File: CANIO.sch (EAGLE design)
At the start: 9 parts

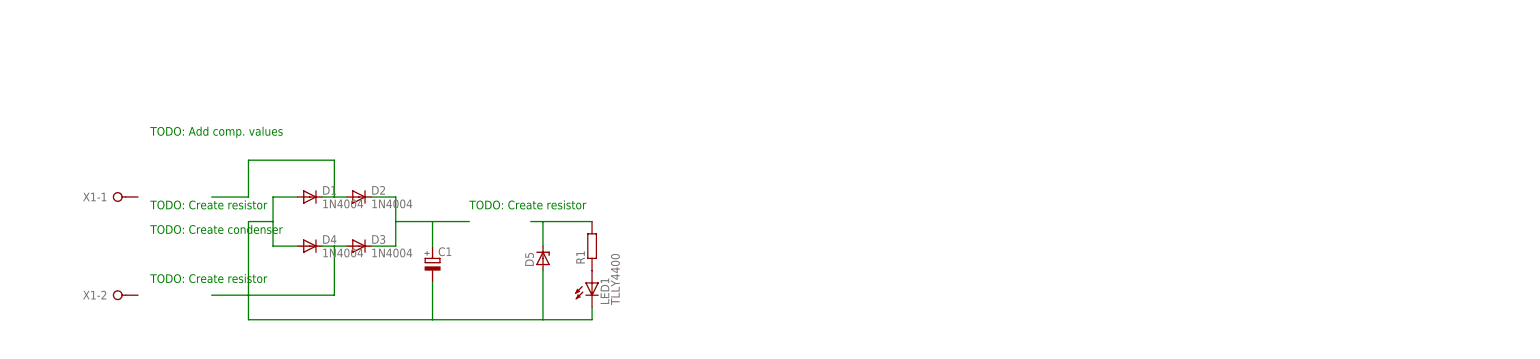
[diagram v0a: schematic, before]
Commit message: adding sensor connector
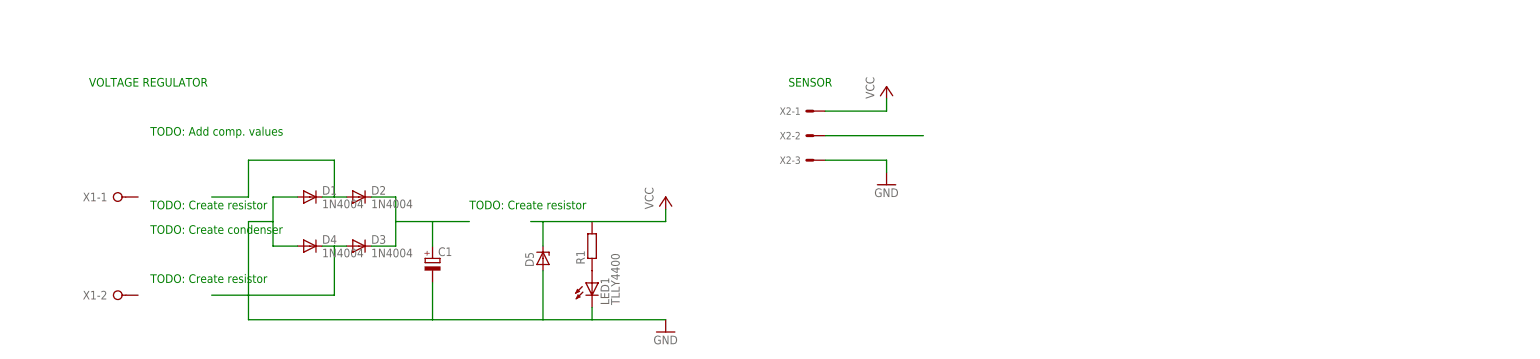
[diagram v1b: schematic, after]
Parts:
- added X2: (no value), con-molex:KK-156-3
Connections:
- removed net N$5: D5.C, R1.2
- new net GND: C1.-, D1.A, D4.A, D5.A, LED1.C, X2-3.S
- new net VCC: D5.C, R1.2, X2-1.S
- net N$4: now also X2-2.S; no longer C1.-, D1.A, D4.A, D5.A, LED1.C
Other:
- note added: "SENSOR"
- note added: "VOLTAGE REGULATOR"
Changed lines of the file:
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@@
 <part name="R1" library="rcl" library_urn="urn:adsk.eagle:library:334" deviceset="R-EU_" device="0204/5"/>
 <part name="LED1" library="led" library_urn="urn:adsk.eagle:library:259" deviceset="TLLY4400" device=""/>
+<part name="P+1" library="supply1" library_urn="urn:adsk.eagle:library:371" deviceset="VCC" device=""/>
+<part name="GND1" library="supply1" library_urn="urn:adsk.eagle:library:371" deviceset="GND" device=""/>
+<part name="X2" library="con-molex" library_urn="urn:adsk.eagle:library:165" deviceset="KK-156-3" device=""/>
+<part name="P+2" library="supply1" library_urn="urn:adsk.eagle:library:371" deviceset="VCC" device=""/>
+<part name="GND2" library="supply1" library_urn="urn:adsk.eagle:library:371" deviceset="GND" device=""/>
 </parts>
 <sheets>
@@
 <text x="76.2" y="40.64" size="1.778" layer="91">TODO: Create resistor</text>
 <text x="10.16" y="55.88" size="1.778" layer="91">TODO: Add comp. values</text>
+<text x="-2.54" y="66.04" size="1.778" layer="91">VOLTAGE REGULATOR</text>
+<text x="142.24" y="66.04" size="1.778" layer="91">SENSOR</text>
 </plain>
 <instances>
@@
 <instance part="R1" gate="G$1" x="101.6" y="33.02" rot="R90"/>
 <instance part="LED1" gate="G$1" x="101.6" y="25.4"/>
+<instance part="P+1" gate="VCC" x="116.84" y="43.18"/>
+<instance part="GND1" gate="1" x="116.84" y="15.24"/>
+<instance part="X2" gate="-1" x="147.32" y="60.96" rot="R180"/>
+<instance part="X2" gate="-2" x="147.32" y="55.88" rot="R180"/>
+<instance part="X2" gate="-3" x="147.32" y="50.8" rot="R180"/>
+<instance part="P+2" gate="VCC" x="162.56" y="66.04"/>
+<instance part="GND2" gate="1" x="162.56" y="45.72"/>
 </instances>
 <busses>
@@
 </segment>
 </net>
-<net name="N$4" class="0">
+<net name="N$6" class="0">
+<segment>
+<pinref part="R1" gate="G$1" pin="1"/>
+<pinref part="LED1" gate="G$1" pin="A"/>
+</segment>
+</net>
+<net name="VCC" class="0">
+<segment>
+<wire x1="88.9" y1="38.1" x2="91.44" y2="38.1" width="0.1524" layer="91"/>
+<wire x1="91.44" y1="38.1" x2="91.44" y2="33.02" width="0.1524" layer="91"/>
+<pinref part="D5" gate="G$1" pin="C"/>
+<pinref part="R1" gate="G$1" pin="2"/>
+<wire x1="101.6" y1="38.1" x2="91.44" y2="38.1" width="0.1524" layer="91"/>
+<pinref part="P+1" gate="VCC" pin="VCC"/>
+<wire x1="101.6" y1="38.1" x2="116.84" y2="38.1" width="0.1524" layer="91"/>
+<wire x1="116.84" y1="38.1" x2="116.84" y2="40.64" width="0.1524" layer="91"/>
+</segment>
+<segment>
+<pinref part="X2" gate="-1" pin="S"/>
+<pinref part="P+2" gate="VCC" pin="VCC"/>
+<wire x1="149.86" y1="60.96" x2="162.56" y2="60.96" width="0.1524" layer="91"/>
+<wire x1="162.56" y1="60.96" x2="162.56" y2="63.5" width="0.1524" layer="91"/>
+</segment>
+</net>
+<net name="GND" class="0">
 <segment>
 <pinref part="D4" gate="1" pin="A"/>
@@
 <wire x1="91.44" y1="17.78" x2="101.6" y2="17.78" width="0.1524" layer="91"/>
 <wire x1="101.6" y1="17.78" x2="101.6" y2="20.32" width="0.1524" layer="91"/>
+<pinref part="GND1" gate="1" pin="GND"/>
+<wire x1="116.84" y1="17.78" x2="101.6" y2="17.78" width="0.1524" layer="91"/>
+</segment>
+<segment>
+<pinref part="X2" gate="-3" pin="S"/>
+<pinref part="GND2" gate="1" pin="GND"/>
+<wire x1="149.86" y1="50.8" x2="162.56" y2="50.8" width="0.1524" layer="91"/>
+<wire x1="162.56" y1="50.8" x2="162.56" y2="48.26" width="0.1524" layer="91"/>
 </segment>
 </net>
-<net name="N$5" class="0">
+<net name="N$4" class="0">
 <segment>
-<wire x1="88.9" y1="38.1" x2="91.44" y2="38.1" width="0.1524" layer="91"/>
-<wire x1="91.44" y1="38.1" x2="91.44" y2="33.02" width="0.1524" layer="91"/>
-<pinref part="D5" gate="G$1" pin="C"/>
-<pinref part="R1" gate="G$1" pin="2"/>
-<wire x1="101.6" y1="38.1" x2="91.44" y2="38.1" width="0.1524" layer="91"/>
+<pinref part="X2" gate="-2" pin="S"/>
+<wire x1="149.86" y1="55.88" x2="170.18" y2="55.88" width="0.1524" layer="91"/>
 </segment>
 </net>
-<net name="N$6" class="0">
-<segment>
-<pinref part="R1" gate="G$1" pin="1"/>
-<pinref part="LED1" gate="G$1" pin="A"/>
-</segment>
-</net>

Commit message: adding sensor robustness and moc3021
Sensor robustness:
+NPN transistor, base from sensor [0-3v]

MOC3021:
+Special protection (ripple) for inductive load
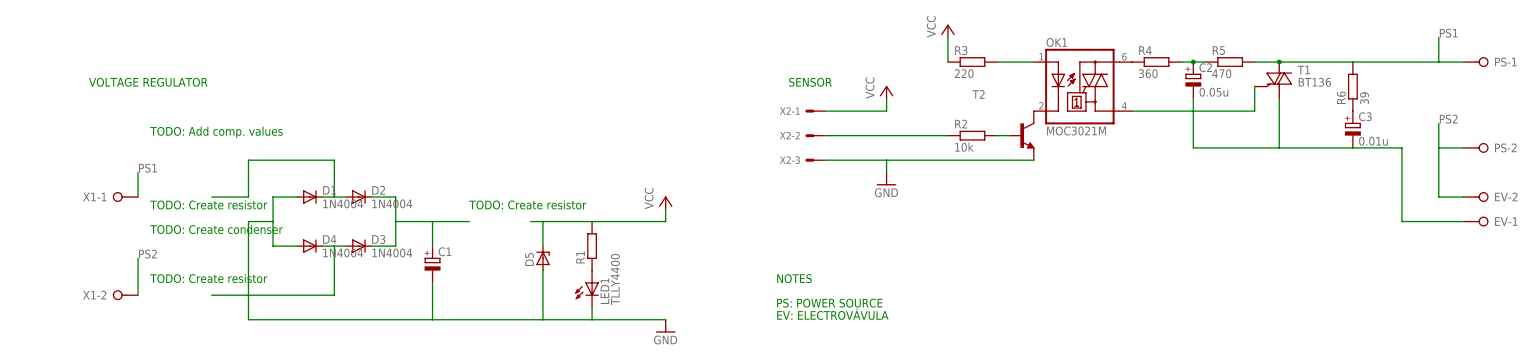
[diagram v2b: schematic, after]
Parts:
- added C2: 0.05u, rcl:CPOL-EUB45181A
- added C3: 0.01u, rcl:CPOL-EUB45181A
- added EV, PS: (no value), con-wago-508:W237-02P
- added OK1: MOC3021M, optocoupler:MOC3021M
- added R2: 10k, resistor:R-EU_0204/7
- added R3: 220, resistor:R-EU_0204/7
- added R4: 360, rcl:R-EU_0204/7
- added R5: 470, rcl:R-EU_0204/7
- added R6: 39, rcl:R-EU_0204/7
- added T1: BT136, triac:BT136
- added T2: (no value), transistor:-NPN-TO92
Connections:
- new net N$10: C2.+, R4.2, R5.1
- new net N$12: OK1.A1, T1.G
- new net N$13: C3.+, R6.1
- new net N$14: C2.-, C3.-, EV-1.KL, T1.A1
- new net N$5: R2.2, T2.B
- new net N$7: OK1.C, T2.C
- new net N$8: OK1.A, R3.2
- new net N$9: OK1.A2, R4.1
- new net PS1: PS-1.KL, R5.2, R6.2, T1.A2, X1-1.KL
- new net PS2: EV-2.KL, PS-2.KL, X1-2.KL
- net GND: now also T2.E
- net N$4: now also R2.1
- net VCC: now also R3.1
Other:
- note added: "EV: ELECTROVÁVULA"
- note added: "NOTES"
- note added: "PS: POWER SOURCE"
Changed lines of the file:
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@@
 <part name="P+2" library="supply1" library_urn="urn:adsk.eagle:library:371" deviceset="VCC" device=""/>
 <part name="GND2" library="supply1" library_urn="urn:adsk.eagle:library:371" deviceset="GND" device=""/>
+<part name="OK1" library="optocoupler" library_urn="urn:adsk.eagle:library:320" deviceset="MOC30*M" device="" technology="21"/>
+<part name="R2" library="resistor" library_urn="urn:adsk.eagle:library:348" deviceset="R-EU_" device="0204/7" value="10k"/>
+<part name="T1" library="triac" library_urn="urn:adsk.eagle:library:403" deviceset="BT136" device=""/>
+<part name="T2" library="transistor" library_urn="urn:adsk.eagle:library:402" deviceset="*-NPN-" device="TO92"/>
+<part name="R3" library="resistor" library_urn="urn:adsk.eagle:library:348" deviceset="R-EU_" device="0204/7" value="220"/>
+<part name="P+3" library="supply1" library_urn="urn:adsk.eagle:library:371" deviceset="VCC" device=""/>
+<part name="R4" library="rcl" library_urn="urn:adsk.eagle:library:334" deviceset="R-EU_" device="0204/7" value="360"/>
+<part name="R5" library="rcl" library_urn="urn:adsk.eagle:library:334" deviceset="R-EU_" device="0204/7" value="470"/>
+<part name="R6" library="rcl" library_urn="urn:adsk.eagle:library:334" deviceset="R-EU_" device="0204/7" value="39"/>
+<part name="C2" library="rcl" library_urn="urn:adsk.eagle:library:334" deviceset="CPOL-EU" device="B45181A" value="0.05u"/>
+<part name="C3" library="rcl" library_urn="urn:adsk.eagle:library:334" deviceset="CPOL-EU" device="B45181A" value="0.01u"/>
+<part name="PS" library="con-wago-508" library_urn="urn:adsk.eagle:library:196" deviceset="W237-02P" device=""/>
+<part name="EV" library="con-wago-508" library_urn="urn:adsk.eagle:library:196" deviceset="W237-02P" device=""/>
 </parts>
 <sheets>
@@
 <text x="-2.54" y="66.04" size="1.778" layer="91">VOLTAGE REGULATOR</text>
 <text x="142.24" y="66.04" size="1.778" layer="91">SENSOR</text>
+<text x="139.7" y="20.32" size="1.778" layer="91">PS: POWER SOURCE</text>
+<text x="139.7" y="25.4" size="1.778" layer="91">NOTES</text>
+<text x="139.7" y="17.78" size="1.778" layer="91">EV: ELECTROVÁVULA</text>
 </plain>
 <instances>
@@
 <instance part="P+2" gate="VCC" x="162.56" y="66.04"/>
 <instance part="GND2" gate="1" x="162.56" y="45.72"/>
+<instance part="OK1" gate="-1" x="203.2" y="66.04"/>
+<instance part="R2" gate="G$1" x="180.34" y="55.88"/>
+<instance part="T1" gate="-1" x="243.84" y="66.04"/>
+<instance part="T2" gate="G$1" x="190.5" y="55.88"/>
+<instance part="R3" gate="G$1" x="180.34" y="71.12"/>
+<instance part="P+3" gate="VCC" x="175.26" y="78.74"/>
+<instance part="R4" gate="G$1" x="218.44" y="71.12"/>
+<instance part="R5" gate="G$1" x="233.68" y="71.12"/>
+<instance part="R6" gate="G$1" x="259.08" y="66.04" rot="R90"/>
+<instance part="C2" gate="G$1" x="226.06" y="68.58"/>
+<instance part="C3" gate="G$1" x="259.08" y="58.42"/>
+<instance part="PS" gate="-1" x="287.02" y="71.12" rot="R180"/>
+<instance part="PS" gate="-2" x="287.02" y="53.34" rot="R180"/>
+<instance part="EV" gate="-1" x="287.02" y="38.1" rot="R180"/>
+<instance part="EV" gate="-2" x="287.02" y="43.18" rot="R180"/>
 </instances>
 <busses>
@@
 <wire x1="149.86" y1="60.96" x2="162.56" y2="60.96" width="0.1524" layer="91"/>
 <wire x1="162.56" y1="60.96" x2="162.56" y2="63.5" width="0.1524" layer="91"/>
+</segment>
+<segment>
+<pinref part="R3" gate="G$1" pin="1"/>
+<pinref part="P+3" gate="VCC" pin="VCC"/>
+<wire x1="175.26" y1="76.2" x2="175.26" y2="71.12" width="0.1524" layer="91"/>
 </segment>
 </net>
@@
 <wire x1="149.86" y1="50.8" x2="162.56" y2="50.8" width="0.1524" layer="91"/>
 <wire x1="162.56" y1="50.8" x2="162.56" y2="48.26" width="0.1524" layer="91"/>
+<pinref part="T2" gate="G$1" pin="E"/>
+<wire x1="193.04" y1="50.8" x2="162.56" y2="50.8" width="0.1524" layer="91"/>
 </segment>
 </net>
@@
 <segment>
 <pinref part="X2" gate="-2" pin="S"/>
-<wire x1="149.86" y1="55.88" x2="170.18" y2="55.88" width="0.1524" layer="91"/>
-</segment>
-</net>
+<wire x1="149.86" y1="55.88" x2="175.26" y2="55.88" width="0.1524" layer="91"/>
+<pinref part="R2" gate="G$1" pin="1"/>
+</segment>
+</net>
+<net name="N$5" class="0">
+<segment>
+<pinref part="R2" gate="G$1" pin="2"/>
+<pinref part="T2" gate="G$1" pin="B"/>
+<wire x1="187.96" y1="55.88" x2="185.42" y2="55.88" width="0.1524" layer="91"/>
+</segment>
+</net>
+<net name="N$7" class="0">
+<segment>
+<pinref part="T2" gate="G$1" pin="C"/>
+<pinref part="OK1" gate="-1" pin="C"/>
+</segment>
+</net>
+<net name="N$8" class="0">
+<segment>
+<pinref part="OK1" gate="-1" pin="A"/>
+<pinref part="R3" gate="G$1" pin="2"/>
+<wire x1="185.42" y1="71.12" x2="193.04" y2="71.12" width="0.1524" layer="91"/>
+</segment>
+</net>
+<net name="N$9" class="0">
+<segment>
+<pinref part="OK1" gate="-1" pin="A2"/>
+<pinref part="R4" gate="G$1" pin="1"/>
+</segment>
+</net>
+<net name="N$10" class="0">
+<segment>
+<pinref part="R4" gate="G$1" pin="2"/>
+<pinref part="R5" gate="G$1" pin="1"/>
+<pinref part="C2" gate="G$1" pin="+"/>
+<pinref part="C2" gate="G$1" pin="+"/>
+<wire x1="228.6" y1="71.12" x2="226.06" y2="71.12" width="0.1524" layer="91"/>
+<junction x="226.06" y="71.12"/>
+<wire x1="226.06" y1="71.12" x2="223.52" y2="71.12" width="0.1524" layer="91"/>
+</segment>
+</net>
+<net name="PS1" class="0">
+<segment>
+<pinref part="R5" gate="G$1" pin="2"/>
+<pinref part="R6" gate="G$1" pin="2"/>
+<wire x1="259.08" y1="71.12" x2="243.84" y2="71.12" width="0.1524" layer="91"/>
+<pinref part="T1" gate="-1" pin="A2"/>
+<wire x1="243.84" y1="71.12" x2="238.76" y2="71.12" width="0.1524" layer="91"/>
+<junction x="243.84" y="71.12"/>
+<pinref part="PS" gate="-1" pin="KL"/>
+<wire x1="281.94" y1="71.12" x2="276.86" y2="71.12" width="0.1524" layer="91"/>
+<wire x1="276.86" y1="71.12" x2="259.08" y2="71.12" width="0.1524" layer="91"/>
+<wire x1="276.86" y1="71.12" x2="276.86" y2="76.2" width="0.1524" layer="91"/>
+<label x="276.86" y="76.2" size="1.778" layer="95"/>
+</segment>
+<segment>
+<pinref part="X1" gate="-1" pin="KL"/>
+<wire x1="7.62" y1="43.18" x2="7.62" y2="48.26" width="0.1524" layer="91"/>
+<label x="7.62" y="48.26" size="1.778" layer="95"/>
+</segment>
+</net>
+<net name="N$12" class="0">
+<segment>
+<pinref part="OK1" gate="-1" pin="A1"/>
+<pinref part="T1" gate="-1" pin="G"/>
+<wire x1="213.36" y1="60.96" x2="238.76" y2="60.96" width="0.1524" layer="91"/>
+<wire x1="238.76" y1="60.96" x2="238.76" y2="66.04" width="0.1524" layer="91"/>
+</segment>
+</net>
+<net name="N$13" class="0">
+<segment>
+<pinref part="R6" gate="G$1" pin="1"/>
+<pinref part="C3" gate="G$1" pin="+"/>
+</segment>
+</net>
+<net name="N$14" class="0">
+<segment>
+<pinref part="C2" gate="G$1" pin="-"/>
+<wire x1="226.06" y1="63.5" x2="226.06" y2="53.34" width="0.1524" layer="91"/>
+<pinref part="C3" gate="G$1" pin="-"/>
+<wire x1="226.06" y1="53.34" x2="243.84" y2="53.34" width="0.1524" layer="91"/>
+<pinref part="T1" gate="-1" pin="A1"/>
+<wire x1="243.84" y1="53.34" x2="259.08" y2="53.34" width="0.1524" layer="91"/>
+<wire x1="243.84" y1="63.5" x2="243.84" y2="53.34" width="0.1524" layer="91"/>
+<pinref part="EV" gate="-1" pin="KL"/>
+<wire x1="281.94" y1="38.1" x2="269.24" y2="38.1" width="0.1524" layer="91"/>
+<wire x1="269.24" y1="38.1" x2="269.24" y2="53.34" width="0.1524" layer="91"/>
+<wire x1="269.24" y1="53.34" x2="259.08" y2="53.34" width="0.1524" layer="91"/>
+</segment>
+</net>
+<net name="PS2" class="0">
+<segment>
+<pinref part="X1" gate="-2" pin="KL"/>
+<wire x1="7.62" y1="22.86" x2="7.62" y2="30.48" width="0.1524" layer="91"/>
+<label x="7.62" y="30.48" size="1.778" layer="95"/>
+</segment>
+<segment>
+<pinref part="EV" gate="-2" pin="KL"/>
+<wire x1="281.94" y1="43.18" x2="276.86" y2="43.18" width="0.1524" layer="91"/>
+<wire x1="276.86" y1="43.18" x2="276.86" y2="53.34" width="0.1524" layer="91"/>
+<pinref part="PS" gate="-2" pin="KL"/>
+<wire x1="276.86" y1="53.34" x2="281.94" y2="53.34" width="0.1524" layer="91"/>
+<wire x1="276.86" y1="53.34" x2="276.86" y2="58.42" width="0.1524" layer="91"/>
+<label x="276.86" y="58.42" size="1.778" layer="95"/>
+</segment>
+</net>

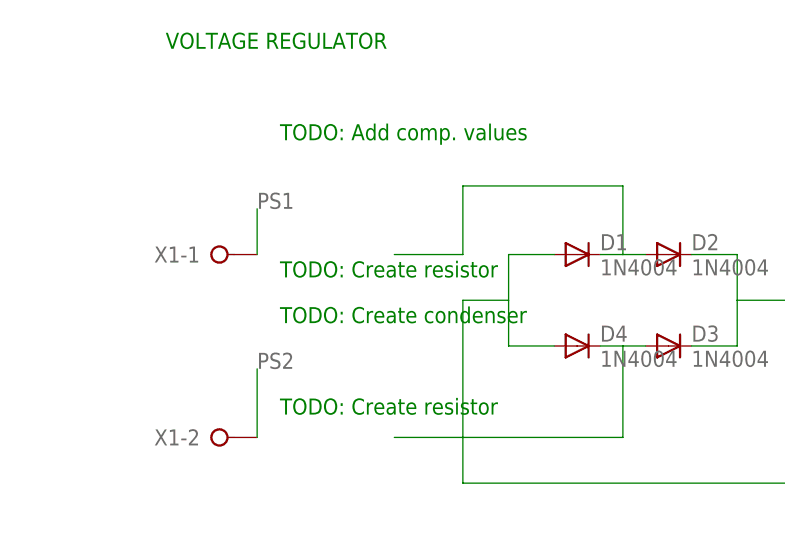
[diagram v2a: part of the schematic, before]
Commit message: Adding Resistor 1w
Created and added library for a new device: Resistor 1K.
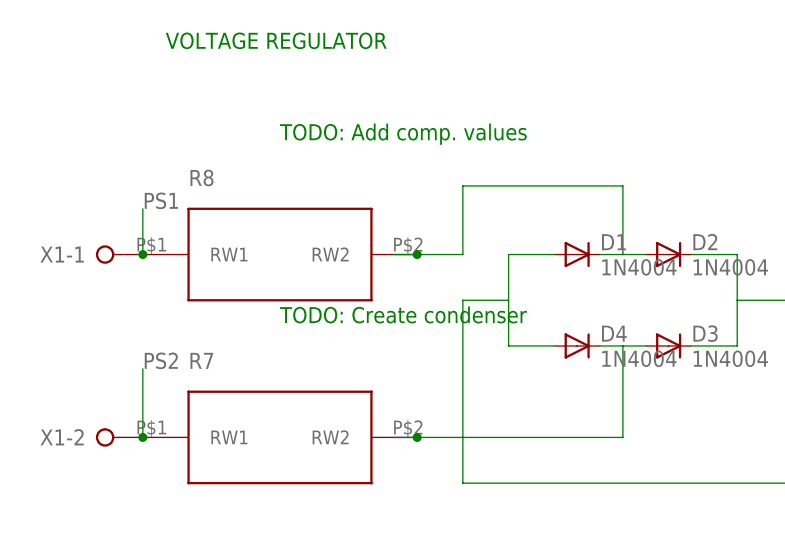
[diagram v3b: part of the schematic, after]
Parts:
- added R7, R8: (no value), Resistor1W:RESISTOR1W
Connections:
- net N$1: now also R7.RW2
- net N$2: now also R8.RW2
- net PS1: now also R8.RW1
- net PS2: now also R7.RW1
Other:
- moved on the sheet: X1-1, X1-2
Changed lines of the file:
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@@
 <part name="PS" library="con-wago-508" library_urn="urn:adsk.eagle:library:196" deviceset="W237-02P" device=""/>
 <part name="EV" library="con-wago-508" library_urn="urn:adsk.eagle:library:196" deviceset="W237-02P" device=""/>
+<part name="R7" library="Resistor1W" deviceset="RESISTOR1W" device=""/>
+<part name="R8" library="Resistor1W" deviceset="RESISTOR1W" device=""/>
 </parts>
 <sheets>
 <sheet>
 <plain>
-<text x="10.16" y="40.64" size="1.778" layer="91">TODO: Create resistor</text>
 <text x="10.16" y="35.56" size="1.778" layer="91">TODO: Create condenser</text>
-<text x="10.16" y="25.4" size="1.778" layer="91">TODO: Create resistor</text>
 <text x="76.2" y="40.64" size="1.778" layer="91">TODO: Create resistor</text>
 <text x="10.16" y="55.88" size="1.778" layer="91">TODO: Add comp. values</text>
@@
 </plain>
 <instances>
-<instance part="X1" gate="-1" x="2.54" y="43.18"/>
-<instance part="X1" gate="-2" x="2.54" y="22.86"/>
+<instance part="X1" gate="-1" x="-10.16" y="43.18"/>
+<instance part="X1" gate="-2" x="-10.16" y="22.86"/>
 <instance part="D1" gate="1" x="43.18" y="43.18"/>
 <instance part="D2" gate="1" x="53.34" y="43.18"/>
@@
 <instance part="EV" gate="-1" x="287.02" y="38.1" rot="R180"/>
 <instance part="EV" gate="-2" x="287.02" y="43.18" rot="R180"/>
+<instance part="R7" gate="G$1" x="10.16" y="22.86"/>
+<instance part="R8" gate="G$1" x="10.16" y="43.18"/>
 </instances>
 <busses>
@@
 <wire x1="30.48" y1="50.8" x2="48.26" y2="50.8" width="0.1524" layer="91"/>
 <wire x1="48.26" y1="50.8" x2="48.26" y2="43.18" width="0.1524" layer="91"/>
-<wire x1="30.48" y1="43.18" x2="22.86" y2="43.18" width="0.1524" layer="91"/>
+<wire x1="30.48" y1="43.18" x2="25.4" y2="43.18" width="0.1524" layer="91"/>
+<pinref part="R8" gate="G$1" pin="RW2"/>
+<wire x1="25.4" y1="43.18" x2="22.86" y2="43.18" width="0.1524" layer="91"/>
+<junction x="25.4" y="43.18"/>
 </segment>
 </net>
@@
 <wire x1="48.26" y1="33.02" x2="50.8" y2="33.02" width="0.1524" layer="91"/>
 <wire x1="48.26" y1="33.02" x2="48.26" y2="22.86" width="0.1524" layer="91"/>
-<wire x1="48.26" y1="22.86" x2="22.86" y2="22.86" width="0.1524" layer="91"/>
+<wire x1="48.26" y1="22.86" x2="25.4" y2="22.86" width="0.1524" layer="91"/>
+<pinref part="R7" gate="G$1" pin="RW2"/>
+<wire x1="25.4" y1="22.86" x2="22.86" y2="22.86" width="0.1524" layer="91"/>
+<junction x="25.4" y="22.86"/>
 </segment>
 </net>
@@
 <pinref part="R5" gate="G$1" pin="1"/>
 <pinref part="C2" gate="G$1" pin="+"/>
-<pinref part="C2" gate="G$1" pin="+"/>
 <wire x1="228.6" y1="71.12" x2="226.06" y2="71.12" width="0.1524" layer="91"/>
 <junction x="226.06" y="71.12"/>
@@
 <segment>
 <pinref part="X1" gate="-1" pin="KL"/>
-<wire x1="7.62" y1="43.18" x2="7.62" y2="48.26" width="0.1524" layer="91"/>
-<label x="7.62" y="48.26" size="1.778" layer="95"/>
+<wire x1="-5.08" y1="43.18" x2="-5.08" y2="48.26" width="0.1524" layer="91"/>
+<label x="-5.08" y="48.26" size="1.778" layer="95"/>
+<pinref part="R8" gate="G$1" pin="RW1"/>
+<junction x="-5.08" y="43.18"/>
 </segment>
 </net>
@@
 <segment>
 <pinref part="X1" gate="-2" pin="KL"/>
-<wire x1="7.62" y1="22.86" x2="7.62" y2="30.48" width="0.1524" layer="91"/>
-<label x="7.62" y="30.48" size="1.778" layer="95"/>
-</segment>
-<segment>
+<wire x1="-5.08" y1="22.86" x2="-5.08" y2="30.48" width="0.1524" layer="91"/>
+<label x="-5.08" y="30.48" size="1.778" layer="95"/>
+<pinref part="R7" gate="G$1" pin="RW1"/>
+<junction x="-5.08" y="22.86"/>
+</segment>
+<segment>
